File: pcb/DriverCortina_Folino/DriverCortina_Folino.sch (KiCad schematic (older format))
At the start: 29 parts, among them J1 AC 220v, J2 Llave Inversora, J3 Motor 1, J4 Motor 2, K1 G3MB-202PL-DC5, K2 G3MB-202PL-DC5, Q1 BC558, Q2 BC558

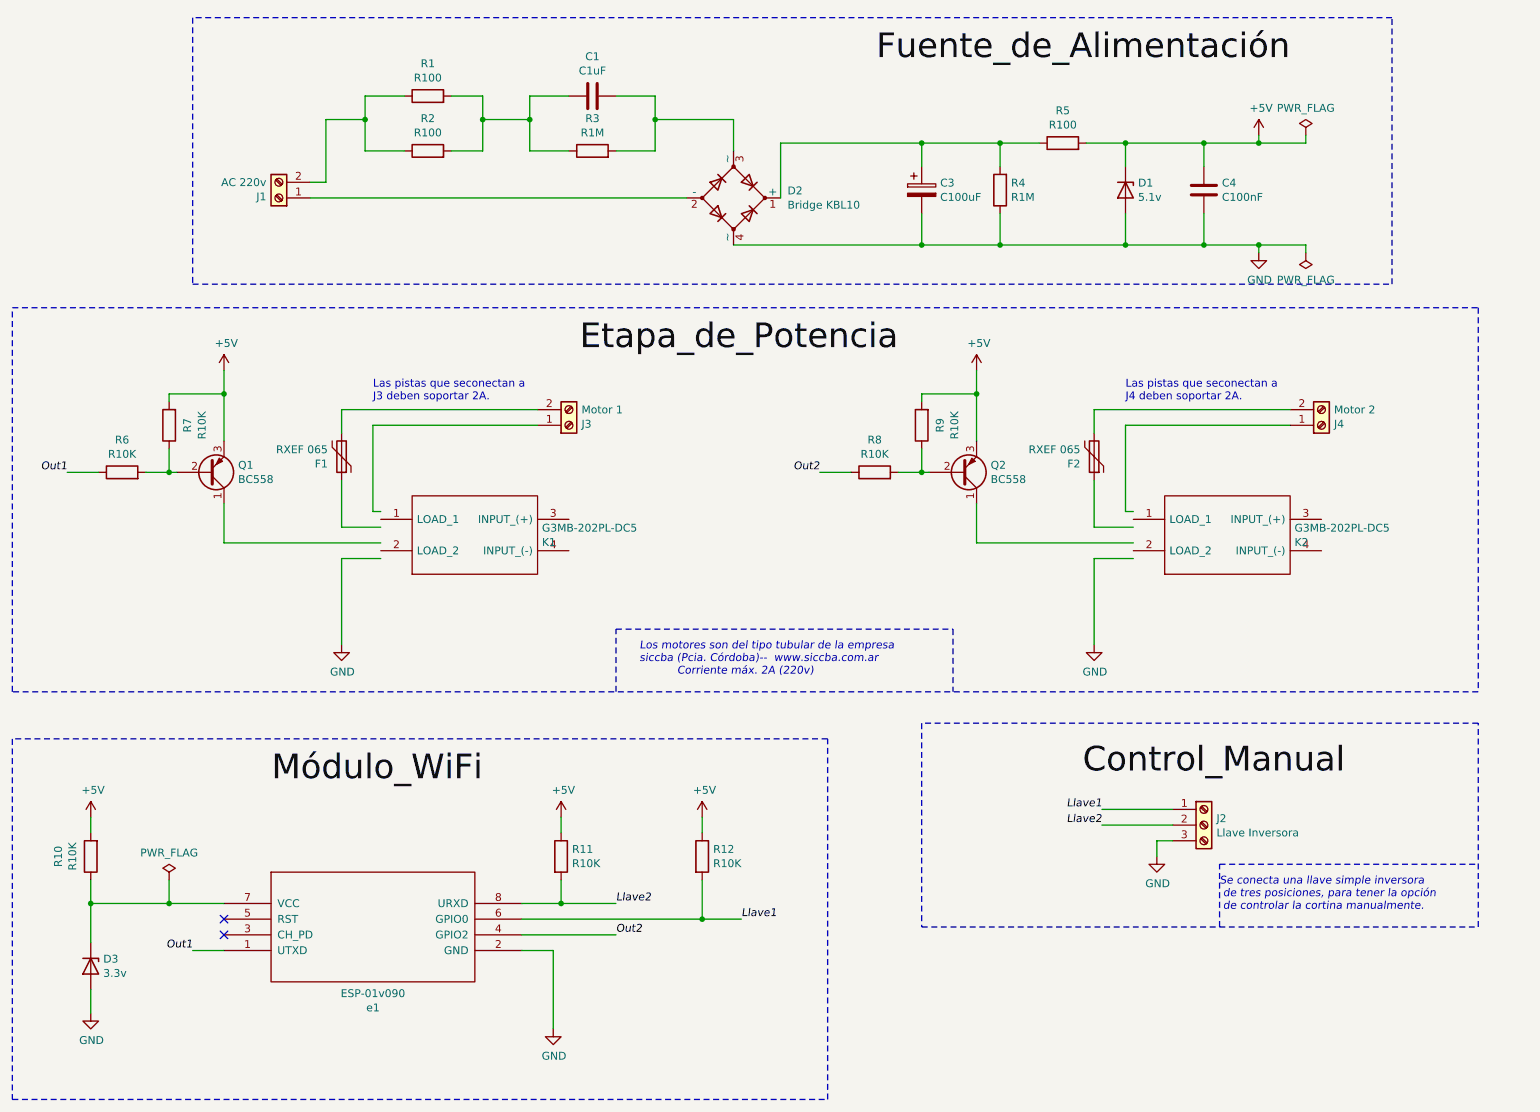
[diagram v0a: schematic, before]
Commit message: Modificación de la organización del repositorio
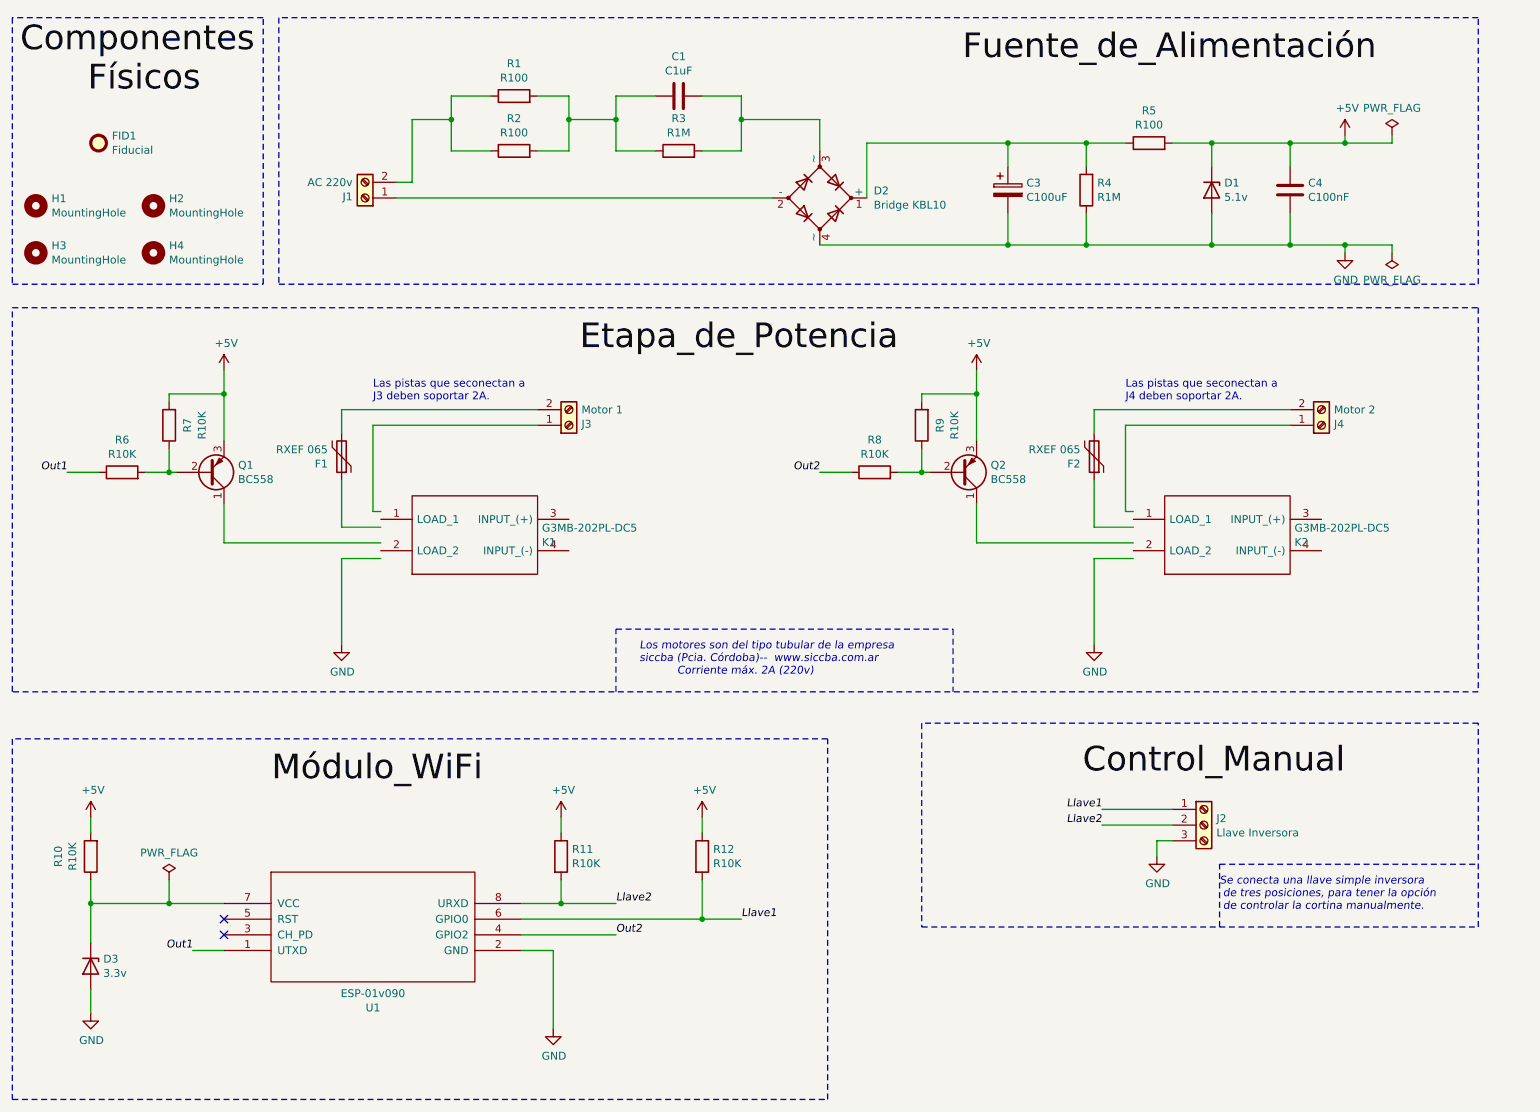
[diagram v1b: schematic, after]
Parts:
- added FID1: Fiducial, Fiducial:Fiducial_1.5mm_Mask3mm, symbol Mechanical:Fiducial
- added H1, H2, H3, H4: MountingHole, MountingHole:MountingHole_2.5mm_Pad, symbol Mechanical:MountingHole
- U1: renamed from e1; Description (none) -> Módulo WiFi; Manufacturer_Name (none) -> Shenzhen Anxinke Technology CO
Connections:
- net labels added: Componentes, Físicos
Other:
- moved on the sheet: C1, C3, C4, D1, D2, J1, R1, R2, R3, R4, R5

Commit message: Actualiza Footprint D3
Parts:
- D3: footprint digikey-footprints:DO-35 -> Diode_THT:D_DO-35_SOD27_P7.62mm_Horizontal
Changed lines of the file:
@@
 F 0 "D3" V 1604 6830 50  0000 L CNN
 F 1 "3.3v" V 1695 6830 50  0000 L CNN
-F 2 "digikey-footprints:DO-35" H 1650 6750 50  0001 C CNN
+F 2 "Diode_THT:D_DO-35_SOD27_P7.62mm_Horizontal" H 1650 6750 50  0001 C CNN
 F 3 "~" H 1650 6750 50  0001 C CNN
 F 4 "Zener de 1/2w" H 1650 6750 50  0001 C CNN "Description"
@@
 Wire Wire Line
 	2500 6350 2150 6350
-Connection ~ 1650 6350
-Wire Wire Line
-	1650 6350 1650 6600
 NoConn ~ 2500 6450
 NoConn ~ 2500 6550
@@
 Wire Wire Line
 	6300 1350 6300 1550
-Wire Wire Line
-	1650 6900 1650 7050
 Wire Wire Line
 	8050 4700 8050 4150
@@
 Text Label 2350 1200 2    157  ~ 0
 Físicos
+Wire Wire Line
+	1650 6600 1650 6350
+Connection ~ 1650 6350
+Wire Wire Line
+	1650 6900 1650 7050
 $EndSCHEMATC
